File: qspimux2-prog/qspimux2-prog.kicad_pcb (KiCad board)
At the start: 4 copper layers, 58 x 38 mm, 96 parts, among them J101 Conn_02x03_Odd_Even, J201 Conn_01x10_MountingPin, J301 Conn_01x03_MountingPin, J401 Conn_01x08_MountingPin, J501 Conn_01x08_MountingPin, J701 USB_B_Micro, J901 Conn_01x03_MountingPin, Q601 BSS138, Q901 FDG6335N, U101 STM32F042C6Tx, U201 SN74LVC1T45DCK, U202 SN74LVC1T45DCK, U203 SN74LVC1T45DCK, U204 SN74LVC1T45DCK, U205 SN74LVC1T45DCK, U206 SN74LVC1T45DCK, U207 SN74LVC1T45DCK, U301 SN74LVC1T45DCK, U302 SN74LVC1T45DCK, U401 TLP176AM, U402 TLP176AM, U403 TLP176AM, U404 TLP176AM, U501 TLP290-4, U601 MIC5504-3.3YM5, U602 AP2127K-ADJ, U701 NUP2202

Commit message: qspimux2-prog: add values for ldo feedback network
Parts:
- C604: value C -> 220p
- R603: value R -> 75k
- R604: value R -> 24k
- R605: value R -> 36k
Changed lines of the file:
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@@
       (effects (font (size 1 1) (thickness 0.15)))
     )
-    (fp_text value "C" (at 0 1.17 90) (layer "F.Fab")
+    (fp_text value "220p" (at 0 1.17 90) (layer "F.Fab")
       (effects (font (size 1 1) (thickness 0.15)))
     )
@@
       (effects (font (size 1 1) (thickness 0.15)))
     )
-    (fp_text value "R" (at 0 1.17 90) (layer "F.Fab")
+    (fp_text value "36k" (at 0 1.17 90) (layer "F.Fab")
       (effects (font (size 1 1) (thickness 0.15)))
     )
@@
       (effects (font (size 1 1) (thickness 0.15)))
     )
-    (fp_text value "R" (at 0 1.17 90) (layer "F.Fab")
+    (fp_text value "24k" (at 0 1.17 90) (layer "F.Fab")
       (effects (font (size 1 1) (thickness 0.15)))
     )
@@
       (effects (font (size 1 1) (thickness 0.15)))
     )
-    (fp_text value "R" (at 0 1.17 90) (layer "F.Fab")
+    (fp_text value "75k" (at 0 1.17 90) (layer "F.Fab")
       (effects (font (size 1 1) (thickness 0.15)))
     )

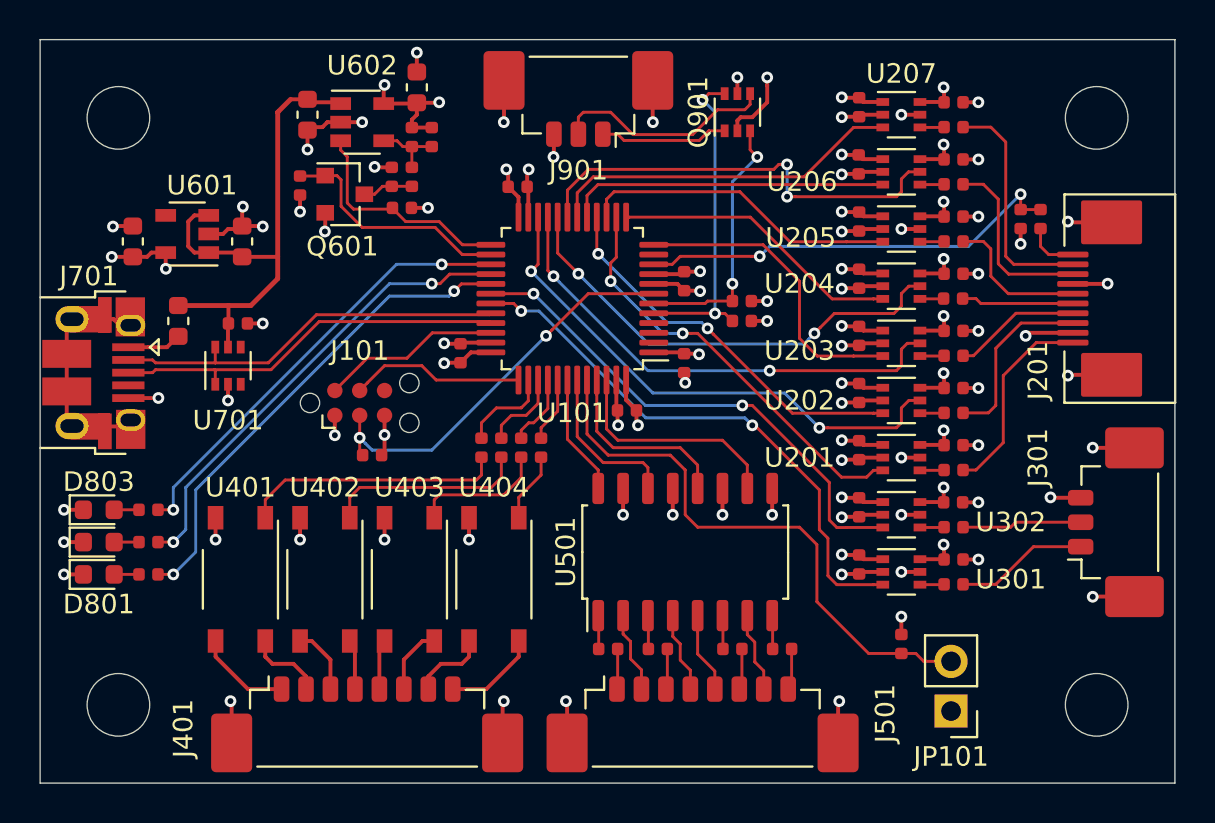
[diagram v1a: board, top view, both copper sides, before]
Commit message: add a few missing capacitors and do some slight layout optimizations
add two missing capacitors on the supply rails of the microcontroller
add capacitor to vtarget monitoringto get a low pass
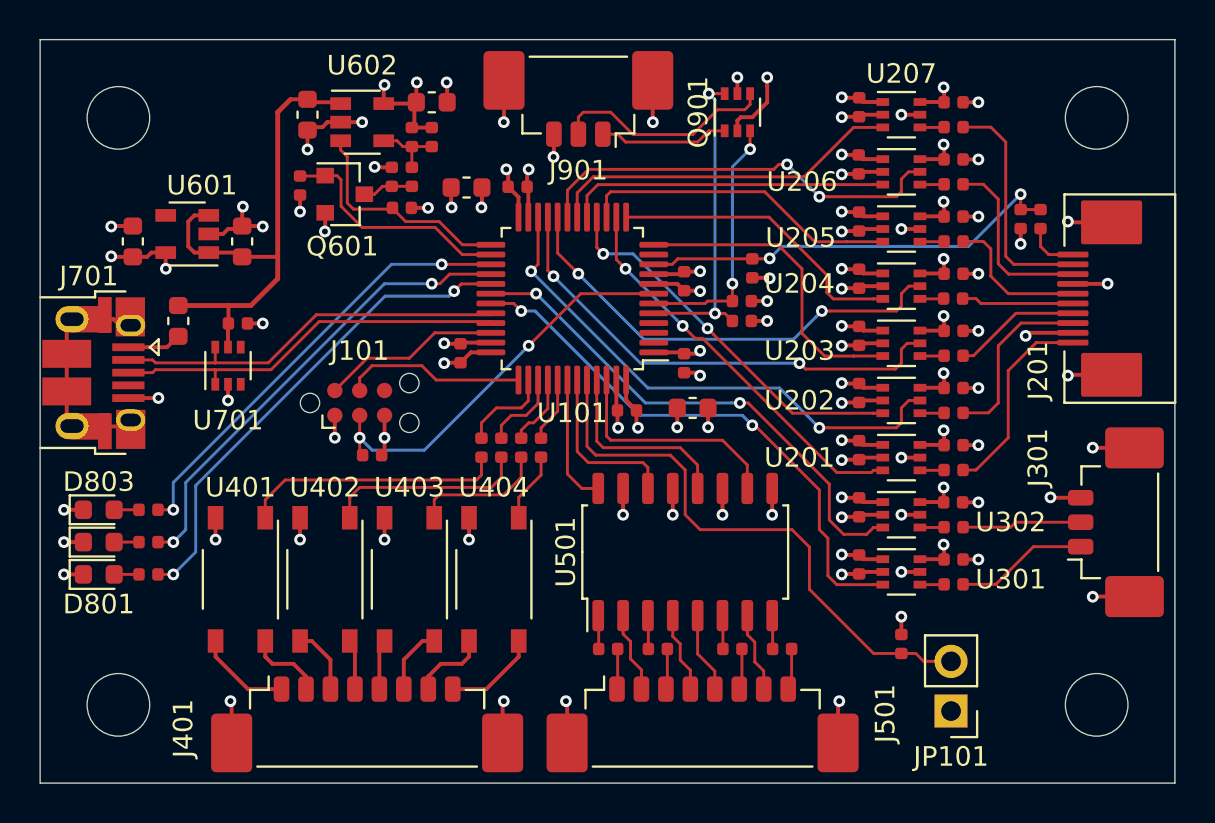
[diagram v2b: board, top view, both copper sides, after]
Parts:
- added C103: 4u7, Capacitor_SMD:C_0603_1608Metric, F.Cu at (121.8, 104.6)
- added C106: 1u, Capacitor_SMD:C_0603_1608Metric, F.Cu at (133.3, 115.8)
- added C215: 100n, Capacitor_SMD:C_0402_1005Metric, F.Cu at (136.4, 108.7)
- moved C605 1.08 mm to (120.0, 100.2), turned to 0 degrees
- renumbered C103 to C104, C104 to C105, C105 to C107, C106 to C108
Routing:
- net GND: track 107.2 -> 110.7 mm, vias 64 -> 67
- net +3V3: track 42.6 -> 45.0 mm, vias 23 -> 25
- net /~CS_A: track 21.6 -> 20.3 mm
- net /IO0_DI_DIR: track 22.5 -> 21.5 mm
- net /IO2_~WP_A: track 14.9 -> 15.4 mm
